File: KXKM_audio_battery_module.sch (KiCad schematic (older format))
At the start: 25 parts, among them J1 Conn_01x06, J11 TEST_1P, J2 TEST_1P, J3 mikroBUS_socket, J4 Conn_01x04, J5 Micro_SD_Card, J6 Conn_01x03, J7 Conn_01x04, Q1 DMN63D8LDW, Q2 DMN63D8LDW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

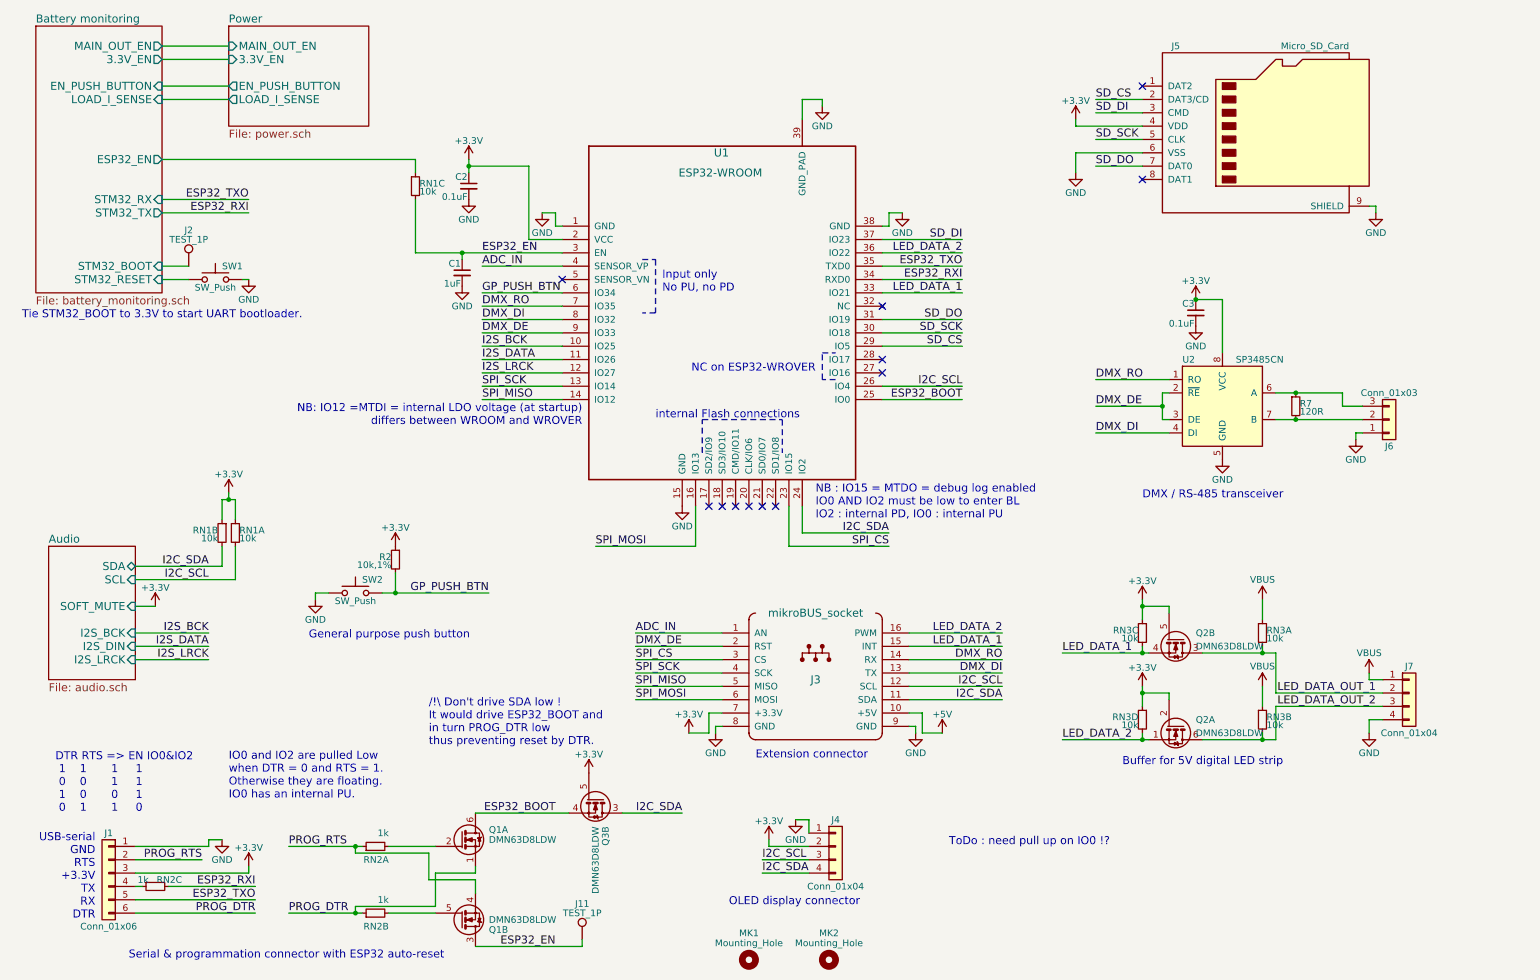
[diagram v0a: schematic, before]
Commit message: v2.0 - audio circuitry on a separate board ; optimized connectors and lots of improvements
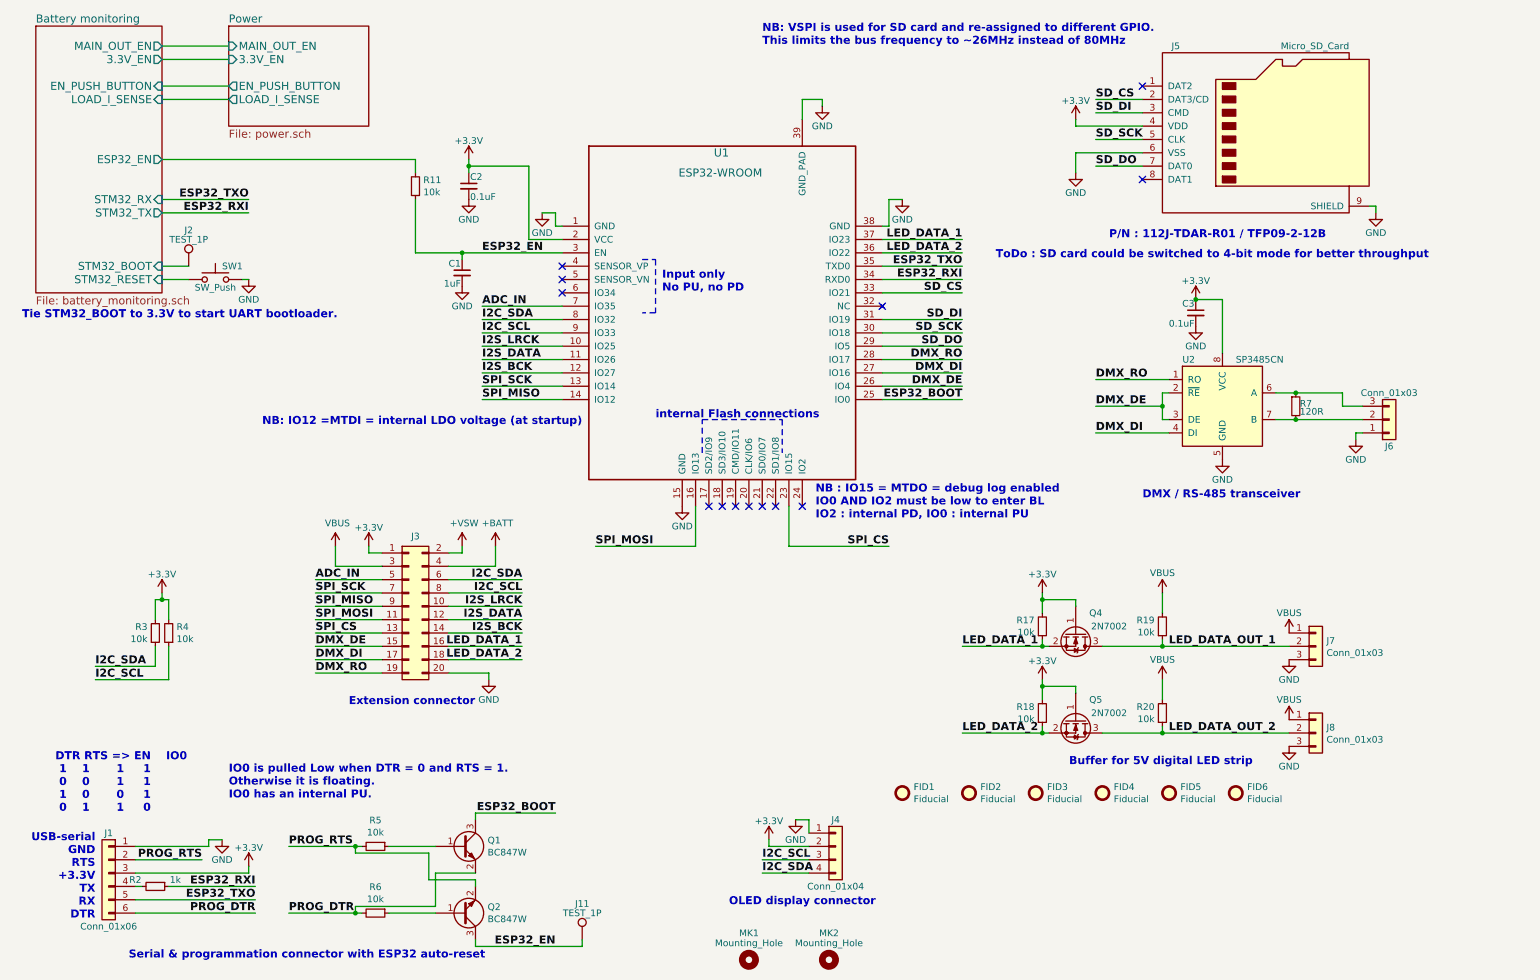
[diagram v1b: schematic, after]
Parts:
- removed J3: mikroBUS_socket, tom_kicad_lib:MIKROBUS_HOST_CONN, symbol KXKM_audio_battery_module-rescue:mikroBUS_socket
- removed J7: Conn_01x04, Pin_Headers:Pin_Header_Straight_1x04_Pitch2.54mm, symbol KXKM_audio_battery_module-rescue:Conn_01x04
- removed Q1, Q2, Q3: DMN63D8LDW, TO_SOT_Packages_SMD:SOT-363_SC-70-6, symbol KXKM_audio_battery_module-rescue:FDG1024NZ
- removed R2: 10k,1%, Resistors_SMD:R_0603, symbol KXKM_audio_battery_module-rescue:R_Small
- removed RN1, RN3: 10k, Resistors_SMD:R_Array_Convex_4x0402, symbol KXKM_audio_battery_module-rescue:R_Pack04_Unit
- removed RN2: 1k, Resistors_SMD:R_Array_Convex_4x0402, symbol KXKM_audio_battery_module-rescue:R_Pack04_Unit
- removed SW2: SW_Push, Buttons_Switches_SMD:SW_SPST_KMR2, symbol KXKM_audio_battery_module-rescue:SW_Push
- added FID1, FID2, FID3, FID4, FID5, FID6: Fiducial, Fiducial:Fiducial_0.5mm_Mask1mm, symbol Mechanical:Fiducial
- added J3: Conn_02x10_Odd_Even, Connector_PinSocket_2.54mm:PinSocket_2x10_P2.54mm_Vertical_SMD, symbol Connector_Generic:Conn_02x10_Odd_Even
- added J7, J8: Conn_01x03, tom_kicad_lib:SolderWirePad_1x03_P3.81mm_Drill1.2mm, symbol Connector_Generic:Conn_01x03
- added Q1, Q2: BC847W, Package_TO_SOT_SMD:SOT-323_SC-70, symbol Transistor_BJT:BC847W
- added Q4, Q5: 2N7002, Package_TO_SOT_SMD:SOT-23, symbol Transistor_FET:2N7002
- added R11, R17, R18, R19, R20, R3, R4, R5, R6: 10k, Resistor_SMD:R_0603_1608Metric, symbol Device:R_Small
- added R2: 1k, Resistor_SMD:R_0603_1608Metric, symbol Device:R_Small
- C1, C2, C3: footprint Capacitors_SMD:C_0603 -> Capacitor_SMD:C_0603_1608Metric
- J1: footprint Pin_Headers:Pin_Header_Straight_1x06_Pitch2.54mm -> Connector_PinHeader_2.54mm:PinHeader_1x06_P2.54mm_Vertical
- J11, J2: footprint Connectors_TestPoints:Test_Point_Pad_d1.5mm -> TestPoint:TestPoint_Pad_D1.5mm
- J4: footprint Pin_Headers:Pin_Header_Straight_1x04_Pitch2.54mm_SMD_Pin1Left -> Connector_PinSocket_2.54mm:PinSocket_1x04_P2.54mm_Vertical
- J6: footprint Pin_Headers:Pin_Header_Straight_1x03_Pitch2.54mm -> Connector_PinHeader_2.54mm:PinHeader_1x03_P2.54mm_Vertical
- MK1, MK2: footprint Mounting_Holes:MountingHole_3.2mm_M3 -> MountingHole:MountingHole_3.2mm_M3
- R7: footprint Resistors_SMD:R_0603 -> Resistor_SMD:R_0603_1608Metric
- SW1: footprint Buttons_Switches_SMD:SW_SPST_KMR2 -> Button_Switch_SMD:SW_SPST_KMR2
- U1: footprint tom_kicad_lib:ESP32-WROOM_WROVER -> RF_Module:ESP32-WROOM-32
- U2: footprint Housings_SOIC:SOIC-8_3.9x4.9mm_Pitch1.27mm -> Package_SO:SOIC-8_3.9x4.9mm_P1.27mm
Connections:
- net +3V3: now also J3.1 (Pin_1), Q4.1 (G), Q5.1 (G), R17.2, R18.2, R3.2, R4.2
- net ADC_IN: now also U1.7 (IO35), J3.5 (Pin_5); no longer U1.4 (SENSOR_VP)
- net Battery monitoring/ESP32_EN: now also R11.2
- net DMX_DE: now also U1.26 (IO4), J3.15 (Pin_15); no longer U1.9 (IO33)
- net DMX_DI: now also U1.27 (IO16), J3.17 (Pin_17); no longer U1.8 (IO32)
- net DMX_RO: now also U1.28 (IO17), J3.19 (Pin_19); no longer U1.7 (IO35)
- net ESP32_BOOT: now also Q1.3 (C)
- net ESP32_EN: now also Q2.3 (C), R11.1
- net ESP32_RXI: now also R2.1
- net GND: now also J3.20 (Pin_20), J7.3 (Pin_3), J8.3 (Pin_3)
- net I2C_SCL: now also U1.9 (IO33), J3.8 (Pin_8), R4.1; no longer U1.26 (IO4)
- net I2C_SDA: now also U1.8 (IO32), J3.6 (Pin_6), R3.1; no longer U1.24 (IO2)
- net I2S_BCK: now also U1.12 (IO27), J3.14 (Pin_14); no longer U1.10 (IO25)
- net I2S_DATA: now also J3.12 (Pin_12)
- net I2S_LRCK: now also U1.10 (IO25), J3.10 (Pin_10); no longer U1.12 (IO27)
- net LED_DATA_1: now also U1.37 (IO23), J3.16 (Pin_16), Q4.2 (S), R17.1; no longer U1.33 (IO21)
- net LED_DATA_2: now also J3.18 (Pin_18), Q5.2 (S), R18.1
- net LED_DATA_OUT_1: now also J7.2 (Pin_2), Q4.3 (D), R19.1
- net LED_DATA_OUT_2: now also J8.2 (Pin_2), Q5.3 (D), R20.1
- net PROG_DTR: now also Q1.2 (E), R6.2
- net PROG_RTS: now also Q2.2 (E), R5.2
- net SD_CS: now also U1.33 (IO21); no longer U1.29 (IO5)
- net SD_DI: now also U1.31 (IO19); no longer U1.37 (IO23)
- net SD_DO: now also U1.29 (IO5); no longer U1.31 (IO19)
- net SPI_CS: now also J3.13 (Pin_13)
- net SPI_MISO: now also J3.9 (Pin_9)
- net SPI_MOSI: now also J3.11 (Pin_11)
- net SPI_SCK: now also J3.7 (Pin_7)
- net VBUS: now also J3.3 (Pin_3), J7.1 (Pin_1), J8.1 (Pin_1), R19.2, R20.2
- net at J1.4 (Pin_4): now also R2.2
- net GP_PUSH_BTN: no longer names the net of U1.6 (IO34)
- new net: Q1.1 (B), R5.1
- new net: Q2.1 (B), R6.1
- new net +BATT: J3.4 (Pin_4)
- new net +VSW: J3.2 (Pin_2)
- no-connect marks 12 -> 13
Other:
- note added: "DTR RTS => EN IO0\n 1 1 1 1\n 0 0 1 1\n 1 0 0 1\n 0 1 1 0"
- note added: "IO0 is pulled Low when DTR = 0 and RTS = 1.\nOtherwise it is floating.\nIO0 has an internal PU."
- note added: "NB: IO12 =MTDI = internal LDO voltage (at startup)"
- note added: "NB: VSPI is used for SD card and re-assigned to different GPIO.\nThis limits the bus frequency to ~~26MHz instead of 80MHz"
- note added: "P/N : 112J-TDAR-R01 / TFP09-2-12B"
- note added: "ToDo : SD card could be switched to 4-bit mode for better throughput"
- note removed: "/!\ Don't drive SDA low ! \nIt would drive ESP32_BOOT and \nin turn PROG_DTR low \nthus preventing reset by DTR."
- note removed: "DTR RTS => EN IO0&IO2\n 1 1 1 1\n 0 0 1 1\n 1 0 0 1\n 0 1 1 0"
- note removed: "General purpose push button"
- note removed: "IO0 and IO2 are pulled Low \nwhen DTR = 0 and RTS = 1.\nOtherwise they are floating.\nIO0 has an internal PU."
- note removed: "NB: IO12 =MTDI = internal LDO voltage (at startup)\ndiffers between WROOM and WROVER"
- note removed: "NC on ESP32-WROVER"
- note removed: "ToDo : need pull up on IO0 !?"
